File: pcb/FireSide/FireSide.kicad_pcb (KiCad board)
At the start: 2 copper layers, 24 parts, among them J1 XT60-Male, J10 Screw_Terminal_Status_LED, J2 Spring_Terminal_Sensor_5V, J3 Spring_Terminal_Sensor_GND, J4 Screw_Terminal_Igniter_A, J5 Screw_Terminal_Igniter_B, J6 Spring_Terminal_A1toA3_SIG, J7 Spring_Terminal_A4toA6_SIG, J8 Spring_Terminal_A1toA3_GND, J9 Spring_Terminal_A4toA6_GND, Q1 2N2222, Q2 IRLZ44N, Q3 2N2222, Q4 IRLZ44N, Q5 2N2222, U1 LM7805ABV

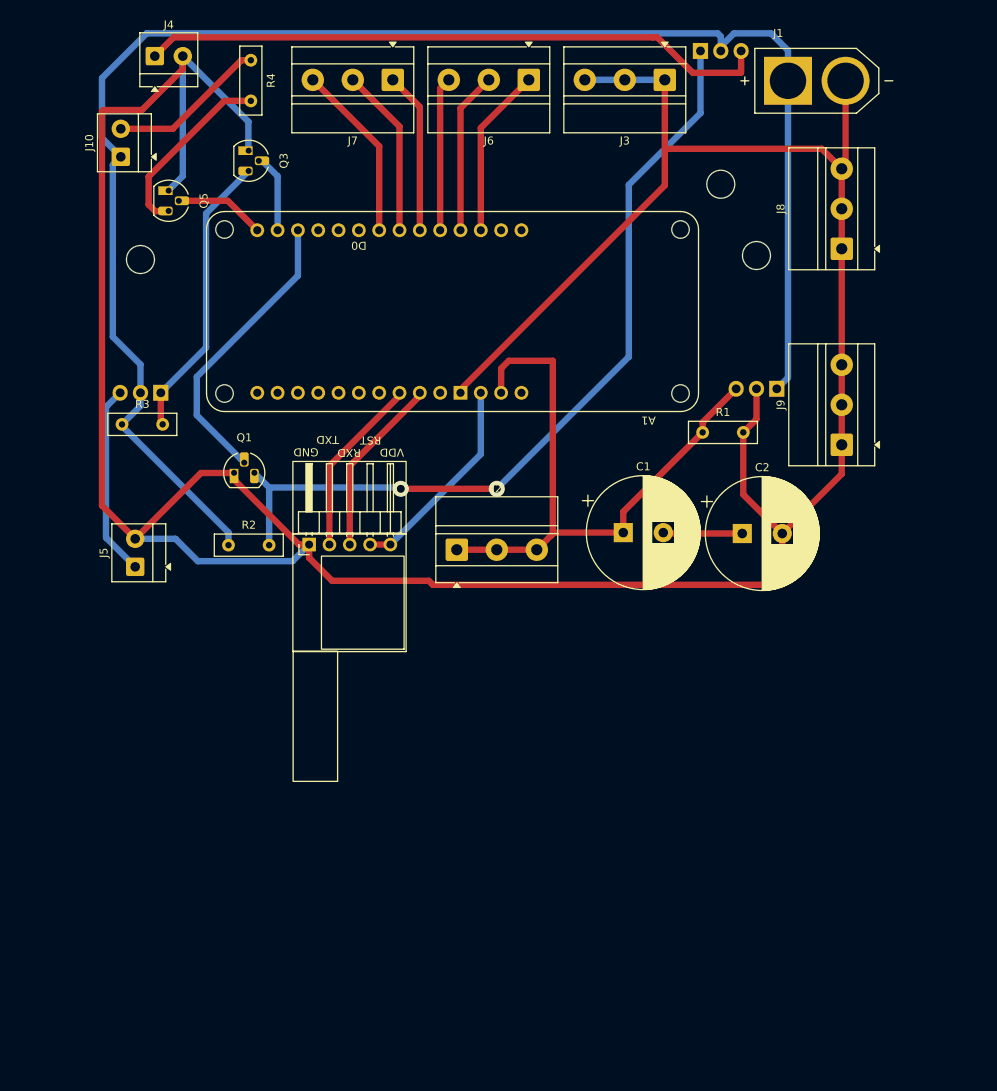
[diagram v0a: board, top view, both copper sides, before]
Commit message: [FS] Update PCB to 120x80 mm and Use JST Connectors
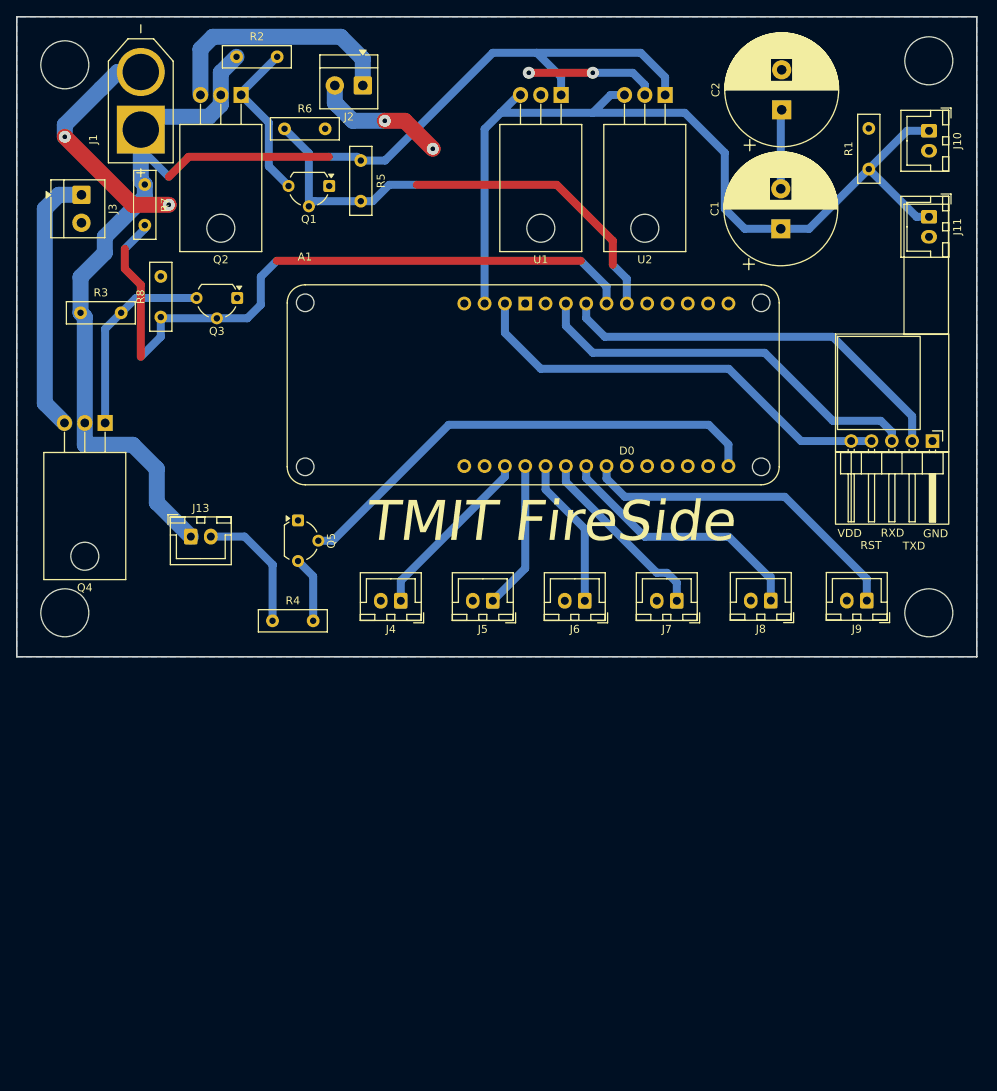
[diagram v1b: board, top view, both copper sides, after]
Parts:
- added J11: 5V_01x02_JST, Connector_JST:JST_XH_B2B-XH-A_1x02_P2.50mm_Vertical, F.Cu at (149.0, 45.5)
- added J13: Status_01x02_JST, Connector_JST:JST_XH_B2B-XH-A_1x02_P2.50mm_Vertical, F.Cu at (56.8, 85.5)
- added R5: 100k, Resistor_THT:R_Box_L8.4mm_W2.5mm_P5.08mm, F.Cu at (78.0, 38.5)
- added R6: 50k, Resistor_THT:R_Box_L8.4mm_W2.5mm_P5.08mm, F.Cu at (68.5, 34.5)
- added R7: 100k, Resistor_THT:R_Box_L8.4mm_W2.5mm_P5.08mm, F.Cu at (51.0, 41.5)
- added R8: 50k, Resistor_THT:R_Box_L8.4mm_W2.5mm_P5.08mm, F.Cu at (53.0, 58.0)
- added U3: ~, RYLR998:RYLR998, F.Cu at (144.5, 68.0)
- J10: value Screw_Terminal_Status_LED -> 5V_01x02_JST; footprint TerminalBlock_MetzConnect:TerminalBlock_MetzConnect_Type059_RT06302HBWC_1x02_P3.50mm_Horizontal -> Connector_JST:JST_XH_B2B-XH-A_1x02_P2.50mm_Vertical
- J2: value Spring_Terminal_Sensor_5V -> Igniter_A_Screws; footprint TerminalBlock_MetzConnect:TerminalBlock_MetzConnect_Type011_RT05503HBLC_1x03_P5.00mm_Horizontal -> TerminalBlock_MetzConnect:TerminalBlock_MetzConnect_Type059_RT06302HBWC_1x02_P3.50mm_Horizontal
- J3: value Spring_Terminal_Sensor_GND -> Igniter_B_Screws; footprint TerminalBlock_MetzConnect:TerminalBlock_MetzConnect_Type011_RT05503HBLC_1x03_P5.00mm_Horizontal -> TerminalBlock_MetzConnect:TerminalBlock_MetzConnect_Type059_RT06302HBWC_1x02_P3.50mm_Horizontal
- J4: value Screw_Terminal_Igniter_A -> A1_01x02_JST; footprint TerminalBlock_MetzConnect:TerminalBlock_MetzConnect_Type059_RT06302HBWC_1x02_P3.50mm_Horizontal -> Connector_JST:JST_XH_B2B-XH-A_1x02_P2.50mm_Vertical
- J5: value Screw_Terminal_Igniter_B -> A2_01x02_JST; footprint TerminalBlock_MetzConnect:TerminalBlock_MetzConnect_Type059_RT06302HBWC_1x02_P3.50mm_Horizontal -> Connector_JST:JST_XH_B2B-XH-A_1x02_P2.50mm_Vertical
- J6: value Spring_Terminal_A1toA3_SIG -> A3_01x02_JST; footprint TerminalBlock_MetzConnect:TerminalBlock_MetzConnect_Type011_RT05503HBLC_1x03_P5.00mm_Horizontal -> Connector_JST:JST_XH_B2B-XH-A_1x02_P2.50mm_Vertical
- J7: value Spring_Terminal_A4toA6_SIG -> A4_01x02_JST; footprint TerminalBlock_MetzConnect:TerminalBlock_MetzConnect_Type011_RT05503HBLC_1x03_P5.00mm_Horizontal -> Connector_JST:JST_XH_B2B-XH-A_1x02_P2.50mm_Vertical
- J8: value Spring_Terminal_A1toA3_GND -> A5_01x02_JST; footprint TerminalBlock_MetzConnect:TerminalBlock_MetzConnect_Type011_RT05503HBLC_1x03_P5.00mm_Horizontal -> Connector_JST:JST_XH_B2B-XH-A_1x02_P2.50mm_Vertical
- J9: value Spring_Terminal_A4toA6_GND -> A6_01x02_JST; footprint TerminalBlock_MetzConnect:TerminalBlock_MetzConnect_Type011_RT05503HBLC_1x03_P5.00mm_Horizontal -> Connector_JST:JST_XH_B2B-XH-A_1x02_P2.50mm_Vertical
- Q1, Q3, Q5: footprint Package_TO_SOT_THT:TO-92_HandSolder -> Package_TO_SOT_THT:TO-92L_Wide
- Q2, Q4, U1: moved to F.Cu
- U2: value ~ -> LM7805ABV; footprint RYLR998:RYLR998 -> Package_TO_SOT_THT:TO-220-3_Horizontal_TabDown
- moved J10 101.1 mm to (149.0, 34.8), turned to -90 degrees
- moved J1 84.5 mm to (50.5, 31.0), turned to 90 degrees
- moved J4 74.7 mm to (83.0, 93.5), turned to 180 degrees
- moved J3 74.3 mm to (43.1, 42.8), turned to -90 degrees
- moved J7 74.2 mm to (117.5, 93.5)
- moved U2 73.3 mm to (116.0, 30.3)
- moved R4 70.1 mm to (67.0, 96.0), turned to 0 degrees
- moved J6 65.5 mm to (106.0, 93.5)
- moved R2 61.1 mm to (62.5, 25.5)
- moved J2 59.2 mm to (78.2, 29.1), turned to 180 degrees
- moved Q2 57.7 mm to (63.0, 30.3), turned to 180 degrees
- moved C2 53.2 mm to (130.6, 32.1), turned to 90 degrees
- moved A1 48.3 mm to (71.0, 56.2), turned to 0 degrees
- moved U1 45.6 mm to (103.0, 30.3)
- moved J5 44.9 mm to (94.5, 93.5), turned to 180 degrees
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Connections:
- A1 pad A1: Net-(J6-Pin_1) -> Net-(J4-Pin_1)
- A1 pad A2: Net-(J6-Pin_2) -> Net-(J5-Pin_1)
- A1 pad A3: Net-(J6-Pin_3) -> Net-(J6-Pin_1)
- A1 pad A5: Net-(J7-Pin_2) -> Net-(J8-Pin_1)
- A1 pad A6: Net-(J7-Pin_3) -> Net-(J9-Pin_1)
- A1 pad D11: unconnected-(A1-D11/SDA-PadD11) -> /FIRE_PIN_A
- A1 pad D12: unconnected-(A1-D12/SCL-PadD12) -> /FIRE_PIN_B
- A1 pad D3: /FIRE_PIN_A -> unconnected-(A1-PadD3)
- A1 pad D4: /FIRE_PIN_B -> unconnected-(A1-PadD4)
- J10 pad 1: +BATT -> /VIN
- J10 pad 2: Net-(J10-Pin_2) -> GND
- J2 pad 1: /VIN -> Net-(J2-Pin_1)
- J2 pad 2: /VIN -> GND
- J3 pad 1: GND -> Net-(J3-Pin_1)
- J6 pad 2: Net-(J6-Pin_2) -> GND
- J7 pad 2: Net-(J7-Pin_2) -> GND
- J8 pad 1: GND -> Net-(J8-Pin_1)
- J9 pad 1: GND -> Net-(J9-Pin_1)
- Q2 pad 3: Net-(J4-Pin_1) -> Net-(J2-Pin_1)
- Q4 pad 3: Net-(J5-Pin_1) -> Net-(J3-Pin_1)
- R4 pad 1: Net-(J10-Pin_2) -> Net-(J13-Pin_2)
- U2 pad 1: Net-(A1-3.3V) -> +BATT
- U2 pad 2: Net-(A1-3.3V) -> GND
- U2 pad 3: Net-(A1-D14/TX) -> /VIN
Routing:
- net GND: track 386.8 -> 63.4 mm, vias 0 -> 6
- net Net-(Q1-C): track 103.6 -> 20.5 mm, vias 2 -> 0
- net /FIRE_PIN_B: track 9.47 -> 88.6 mm, vias 0 -> 5
- net Net-(J4-Pin_1): track 78.8 -> 22.2 mm
- net /STATUS_PIN: track 10.9 -> 61.0 mm
- net Net-(J9-Pin_1): track 0.00 -> 42.4 mm
- net +BATT: track 204.4 -> 167.9 mm, vias 0 -> 2
- net /VIN: track 77.3 -> 111.6 mm
- net Net-(J3-Pin_1): track 0.00 -> 33.1 mm
- net Net-(J8-Pin_1): track 0.00 -> 32.4 mm
- net Net-(J2-Pin_1): track 0.00 -> 31.1 mm
- net Net-(A1-3.3V): track 26.2 -> 55.1 mm
- net Net-(A1-D13/RX): track 22.6 -> 50.8 mm
- net Net-(A1-D14/TX): track 22.6 -> 50.2 mm
- net /FIRE_PIN_A: track 36.6 -> 61.5 mm, vias 0 -> 2
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- added copper zone on B.Cu, net GND
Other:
- board outline added: 120 x 80 mm
- board text added: "TMIT FireSide"

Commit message: [FS] Transition PCB to Nucleo L412KB and SMD Components
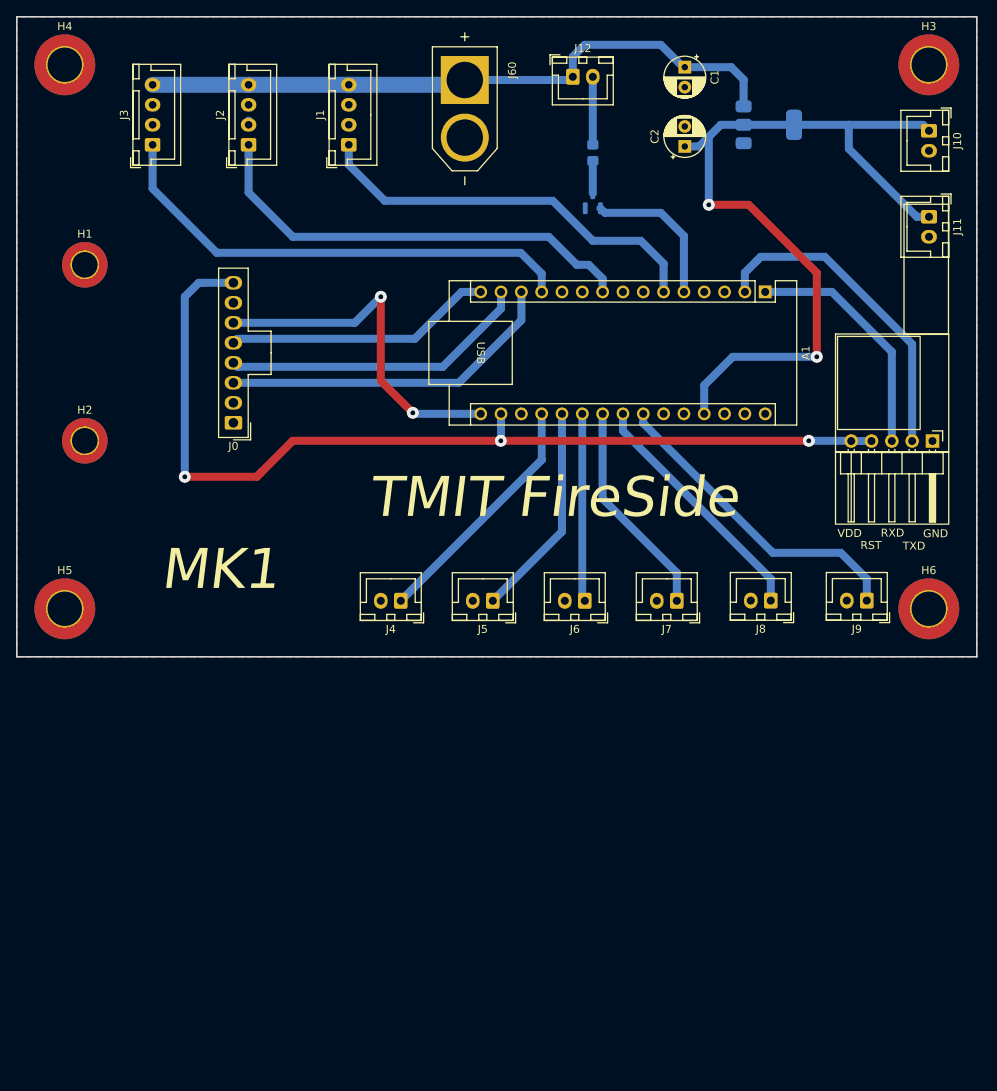
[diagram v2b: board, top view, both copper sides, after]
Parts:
- removed J13: Status_01x02_JST, Connector_JST:JST_XH_B2B-XH-A_1x02_P2.50mm_Vertical
- removed Q2, Q4: IRLZ44N, Package_TO_SOT_THT:TO-220-3_Horizontal_TabDown
- removed Q3, Q5: 2N2222, Package_TO_SOT_THT:TO-92L_Wide
- removed R2, R3, R4: 1k, Resistor_THT:R_Box_L8.4mm_W2.5mm_P5.08mm
- removed R5, R7: 100k, Resistor_THT:R_Box_L8.4mm_W2.5mm_P5.08mm
- removed R6, R8: 50k, Resistor_THT:R_Box_L8.4mm_W2.5mm_P5.08mm
- removed U2: LM7805ABV, Package_TO_SOT_THT:TO-220-3_Horizontal_TabDown
- added H1: SDModuleM3, MountingHole:MountingHole_3.2mm_M3_ISO7380_Pad_TopBottom, F.Cu at (43.5, 51.5)
- added H2: SDModuleM3, MountingHole:MountingHole_3.2mm_M3_ISO7380_Pad_TopBottom, F.Cu at (43.5, 73.5)
- added H3: BoardM4, MountingHole:MountingHole_4.3mm_M4_ISO7380_Pad_TopBottom, F.Cu at (149.0, 26.5)
- added H4: BoardM4, MountingHole:MountingHole_4.3mm_M4_ISO7380_Pad_TopBottom, F.Cu at (41.0, 26.5)
- added H5: BoardM4, MountingHole:MountingHole_4.3mm_M4_ISO7380_Pad_TopBottom, F.Cu at (41.0, 94.5)
- added H6: BoardM4, MountingHole:MountingHole_4.3mm_M4_ISO7380_Pad_TopBottom, F.Cu at (149.0, 94.5)
- added J0: SDIOModule, Connector_Molex:Molex_Nano-Fit_105309-xx08_1x08_P2.50mm_Vertical, F.Cu at (62.1, 71.2)
- added J12: Status_01x02_JST, Connector_JST:JST_XH_B2B-XH-A_1x02_P2.50mm_Vertical, F.Cu at (104.5, 28.0)
- added J60: XT60-Male, XT60-M:AMASS_XT60-M, F.Cu at (91.0, 32.0)
- A1: value Arduino_MKR_Zero -> Nucleo-L412KB; footprint PCM_arduino-library:Arduino_MKR_Zero_Socket -> Module:Arduino_Nano
- C1, C2: value 15F -> 22u; footprint Capacitor_THT:CP_Radial_D14.0mm_P5.00mm -> Capacitor_THT:CP_Radial_D5.0mm_P2.50mm
- J1: value XT60-Male -> D4184_PIN_A; footprint XT60-M:AMASS_XT60-M -> Connector_JST:JST_XH_B4B-XH-A_1x04_P2.50mm_Vertical
- J2: value Igniter_A_Screws -> D4184_PIN_B; footprint TerminalBlock_MetzConnect:TerminalBlock_MetzConnect_Type059_RT06302HBWC_1x02_P3.50mm_Horizontal -> Connector_JST:JST_XH_B4B-XH-A_1x04_P2.50mm_Vertical
- J3: value Igniter_B_Screws -> D4184_PIN_C; footprint TerminalBlock_MetzConnect:TerminalBlock_MetzConnect_Type059_RT06302HBWC_1x02_P3.50mm_Horizontal -> Connector_JST:JST_XH_B4B-XH-A_1x04_P2.50mm_Vertical
- J4: value A1_01x02_JST -> A0_01x02_JST
- J5: value A2_01x02_JST -> A1_01x02_JST
- J6: value A3_01x02_JST -> A2_01x02_JST
- J7: value A4_01x02_JST -> A3_01x02_JST
- J8: value A5_01x02_JST -> A4_01x02_JST
- J9: value A6_01x02_JST -> A5_01x02_JST
- Q1: value 2N2222 -> MMBT2222A; footprint Package_TO_SOT_THT:TO-92L_Wide -> Package_TO_SOT_SMD:SOT-23; moved to B.Cu
- R1: footprint Resistor_THT:R_Box_L8.4mm_W2.5mm_P5.08mm -> Resistor_SMD:R_0805_2012Metric_Pad1.20x1.40mm_HandSolder; moved to B.Cu
- U1: value LM7805ABV -> AMS1117-5.0; footprint Package_TO_SOT_THT:TO-220-3_Horizontal_TabDown -> Package_TO_SOT_SMD:SOT-223-3_TabPin2; moved to B.Cu
- U3: value ~ -> RYLR998
- moved A1 57.5 mm to (128.6, 54.9), turned to -90 degrees
- moved R1 34.6 mm to (107.0, 37.5), turned to -90 degrees
- moved Q1 33.0 mm to (107.0, 43.5), turned to 90 degrees
- moved J1 26.6 mm to (76.5, 36.5)
- moved U1 26.2 mm to (129.0, 34.0), turned to 0 degrees
- moved C1 23.5 mm to (118.5, 26.8), turned to -90 degrees
- moved J2 16.1 mm to (64.0, 36.5), turned to 90 degrees
- moved C2 12.9 mm to (118.5, 36.7)
- moved J3 10.9 mm to (52.0, 36.5), turned to 90 degrees
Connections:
- C1 pad 1: /VIN -> +BATT
- C1 pad 2: Net-(C1-Pad2) -> GND
- C2 pad 1: Net-(C1-Pad2) -> /5VIN
- J10 pad 1: /VIN -> /5VIN
- J11 pad 1: /VIN -> /5VIN
- J2 pad 1: Net-(J2-Pin_1) -> /FIRE_PIN_B
- J3 pad 1: Net-(J3-Pin_1) -> /FIRE_PIN_C
- J4 pad 1: Net-(J4-Pin_1) -> Net-(A1-A0)
- J5 pad 1: Net-(J5-Pin_1) -> Net-(A1-A1)
- J6 pad 1: Net-(J6-Pin_1) -> Net-(A1-A2)
- J7 pad 1: Net-(J7-Pin_1) -> Net-(A1-A3)
- J8 pad 1: Net-(J8-Pin_1) -> Net-(A1-SDA/A4)
- J9 pad 1: Net-(J9-Pin_1) -> Net-(A1-SCL/A5)
- Q1 pad 1: GND -> /STATUS_PIN
- Q1 pad 2: /FIRE_PIN_A -> GND
- R1 pad 1: /VIN -> Net-(J12-Pin_2)
- R1 pad 2: GND -> Net-(Q1-C)
- U1 pad 1: +BATT -> GND
- U1 pad 2: GND -> /5VIN
- U1 pad 3: /VIN -> +BATT
- U3 pad 1: Net-(A1-3.3V) -> Net-(A1-3V3)
- U3 pad 2: Net-(A1-3.3V) -> Net-(A1-3V3)
- U3 pad 3: Net-(A1-D14/TX) -> Net-(A1-TX1)
- U3 pad 4: Net-(A1-D13/RX) -> Net-(A1-RX1)
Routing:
- net Net-(A1-3V3): track 0.00 -> 120.4 mm, vias 0 -> 3
- net /VIN: track 111.6 -> 0.00 mm
- net /5VIN: track 0.00 -> 103.6 mm, vias 0 -> 2
- net +BATT: track 167.9 -> 82.6 mm, vias 2 -> 0
- net GND: track 63.4 -> 0.55 mm, vias 6 -> 0
- net /FIRE_PIN_C: track 0.00 -> 60.8 mm
- net Net-(A1-3.3V): track 55.1 -> 0.00 mm
- net Net-(A1-D13/RX): track 50.8 -> 0.00 mm
- net Net-(A1-D14/TX): track 50.2 -> 0.00 mm
- net Net-(A1-SCK): track 0.00 -> 44.5 mm, vias 0 -> 2
- net Net-(A1-D10): track 0.00 -> 42.8 mm
- net Net-(J9-Pin_1): track 42.4 -> 0.00 mm
- net /STATUS_PIN: track 61.0 -> 18.9 mm
- net Net-(A1-RX1): track 0.00 -> 40.8 mm
- net Net-(A1-SCL/A5): track 0.00 -> 39.9 mm
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- added copper zone on F.Cu, net GND
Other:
- outline, holes or cut-outs redrawn
- board text added: "MK1"
